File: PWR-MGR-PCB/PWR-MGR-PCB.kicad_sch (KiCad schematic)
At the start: 23 parts, among them J1 USB_C_Receptacle_USB2.0_14P, J2 Battery_1x2, U1 USBLC6-2SC6, U3 BQ24074RGT, U4 TPS631011YBGR

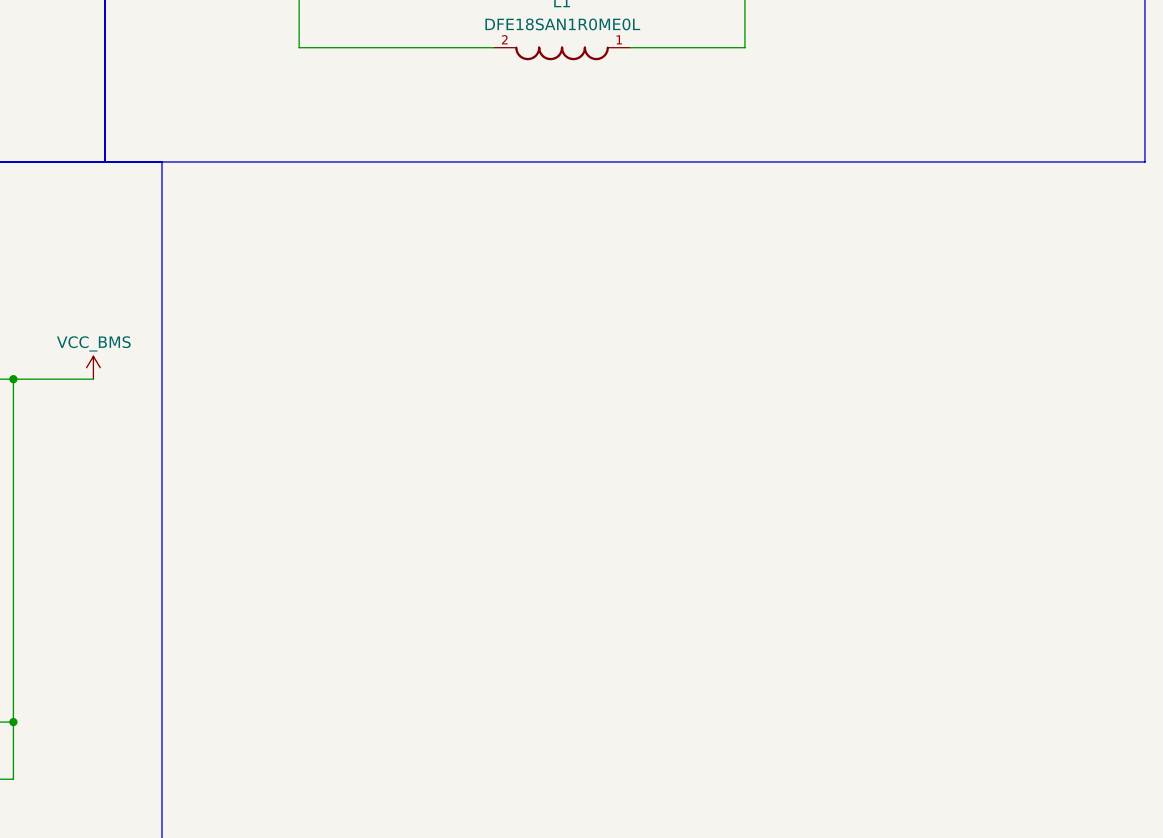
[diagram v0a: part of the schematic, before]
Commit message: Add USB lines, add mount holes, add power port
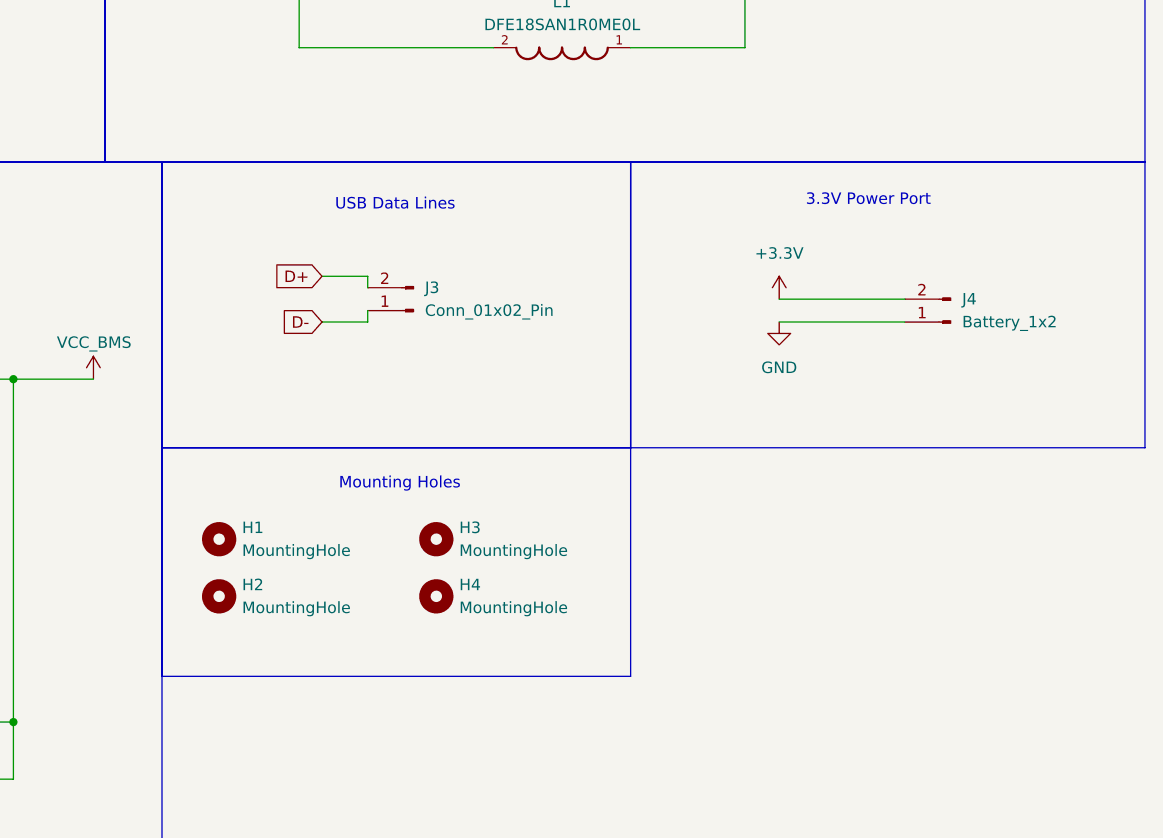
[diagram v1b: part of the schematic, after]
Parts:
- added H1, H2, H3, H4: MountingHole, MountingHole:MountingHole_2.1mm, symbol Mechanical:MountingHole
- added J3: Conn_01x02_Pin, Connector_PinHeader_1.00mm:PinHeader_1x02_P1.00mm_Vertical_SMD_Pin1Right, symbol Connector:Conn_01x02_Pin
- added J4: Battery_1x2, Connector_JST:JST_PH_B2B-PH-K_1x02_P2.00mm_Vertical, symbol Connector:Conn_01x02_Pin
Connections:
- net +3.3V: now also J4.2 (Pin_2)
- net D+: now also J3.2 (Pin_2)
- net D-: now also J3.1 (Pin_1)
- net GND: now also J4.1 (Pin_1)
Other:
- note added: "3.3V Power Port"
- note added: "Mounting Holes"
- note added: "USB Data Lines"

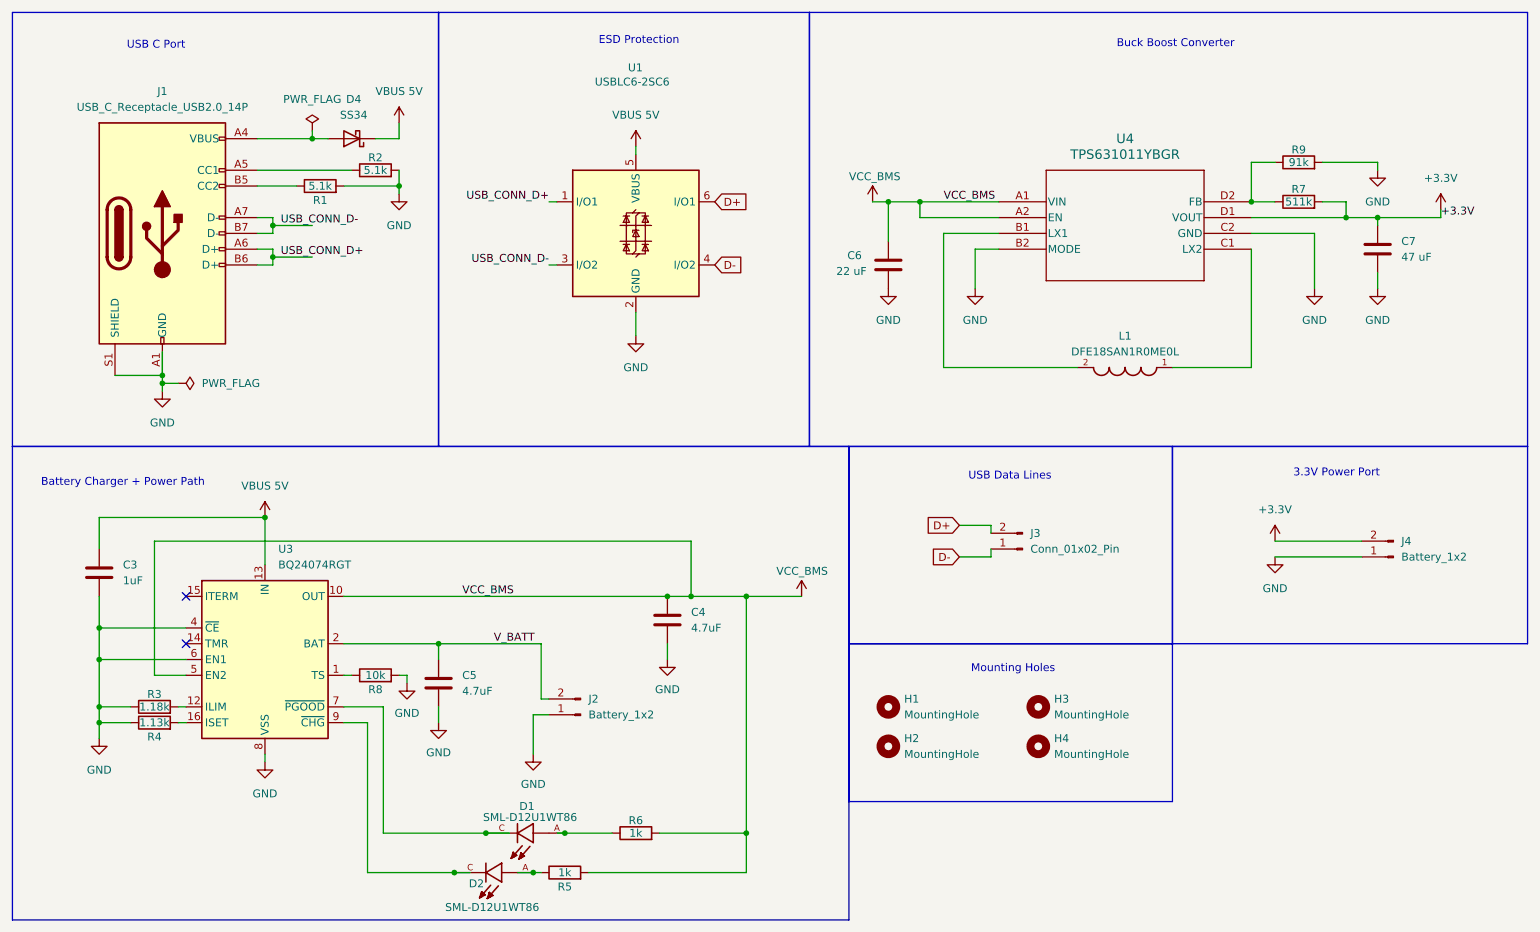
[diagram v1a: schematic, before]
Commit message: Format sheet for reusability
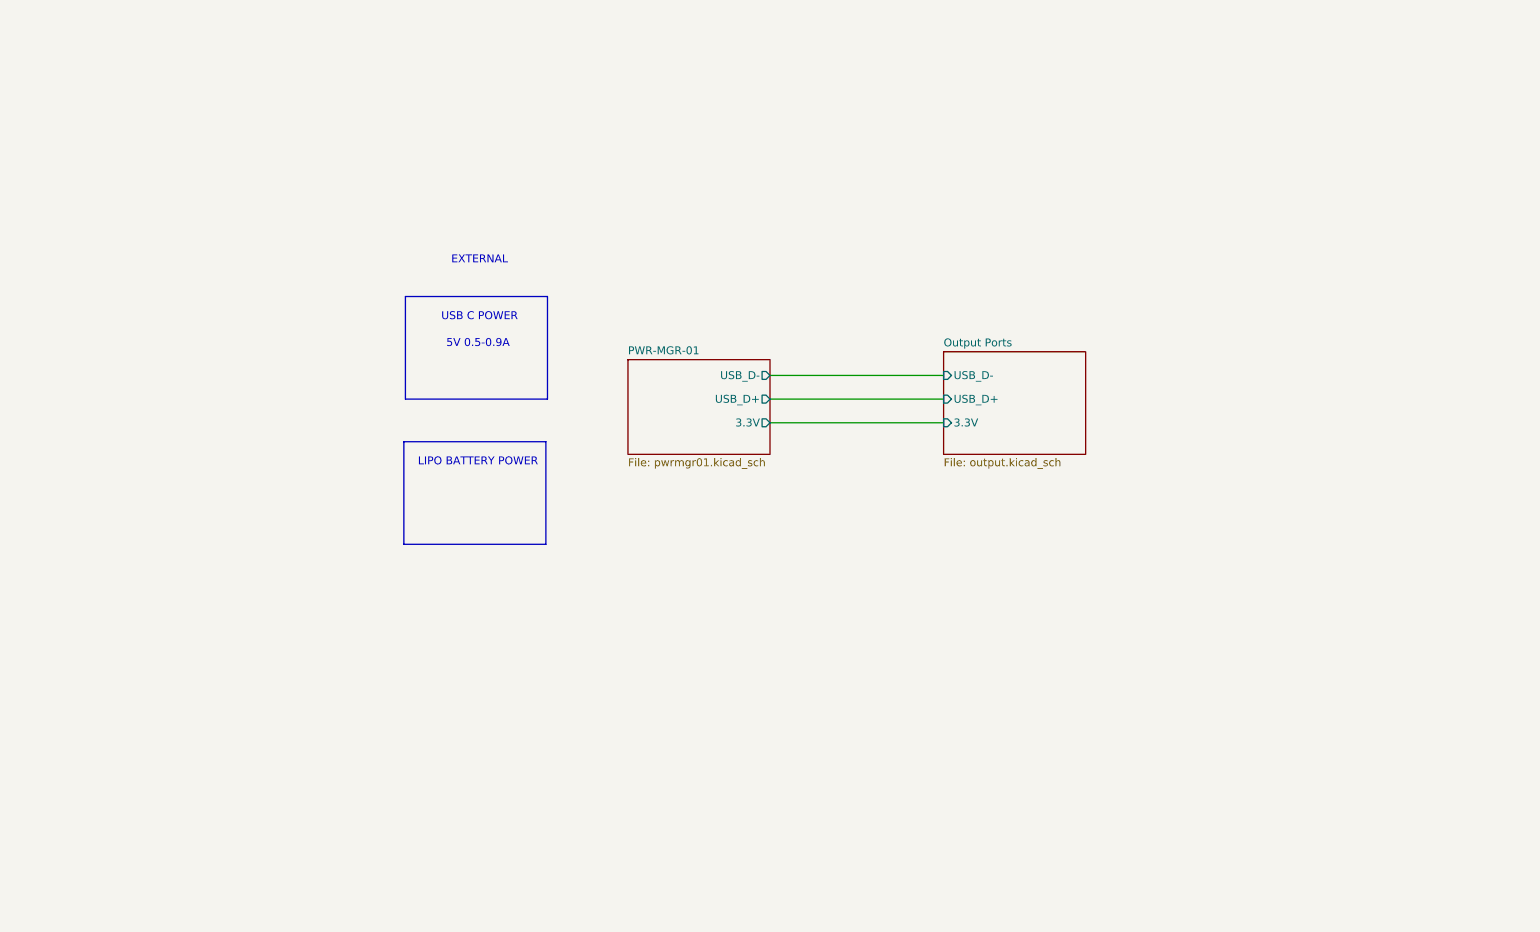
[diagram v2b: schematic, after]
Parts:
- removed C3: 1uF, Capacitor_SMD:C_0805_2012Metric, symbol Device:C
- removed C4, C5: 4.7uF, Capacitor_SMD:C_0805_2012Metric, symbol Device:C
- removed C6: 22 uF, Capacitor_SMD:C_0805_2012Metric, symbol Device:C
- removed C7: 47 uF, Capacitor_SMD:C_0805_2012Metric, symbol Device:C
- removed D1, D2: SML-D12U1WT86, LED - SML_D12U1WT86:LED_SML-D12U1WT86, symbol SML-D12U1WT86:SML-D12U1WT86
- removed D4: SS34, Diode_SMD:D_SMA, symbol Diode:SS34
- removed H1, H2, H3, H4: MountingHole, MountingHole:MountingHole_2.1mm, symbol Mechanical:MountingHole
- removed J1: USB_C_Receptacle_USB2.0_14P, Connector_USB:USB_C_Receptacle_GCT_USB4105-xx-A_16P_TopMnt_Horizontal, symbol Connector:USB_C_Receptacle_USB2.0_14P
- removed J2, J4: Battery_1x2, Connector_JST:JST_PH_B2B-PH-K_1x02_P2.00mm_Vertical, symbol Connector:Conn_01x02_Pin
- removed J3: Conn_01x02_Pin, Connector_PinHeader_1.00mm:PinHeader_1x02_P1.00mm_Vertical_SMD_Pin1Right, symbol Connector:Conn_01x02_Pin
- removed L1: DFE18SAN1R0ME0L, DFE18SAN1ROMEO Inductor:INDC1608X80N, symbol DFE18SAN1R0ME0L:DFE18SAN1R0ME0L
- removed R1, R2: 5.1k, Resistor_SMD:R_0805_2012Metric, symbol Device:R
- removed R3: 1.18k, Resistor_SMD:R_0805_2012Metric, symbol Device:R
- removed R4: 1.13k, Resistor_SMD:R_0805_2012Metric, symbol Device:R
- removed R5, R6: 1k, Resistor_SMD:R_0805_2012Metric, symbol Device:R
- removed R7: 511k, Resistor_SMD:R_0805_2012Metric, symbol Device:R
- removed R8: 10k, Resistor_SMD:R_0805_2012Metric, symbol Device:R
- removed R9: 91k, Resistor_SMD:R_0805_2012Metric, symbol Device:R
- removed U1: USBLC6-2SC6, Package_TO_SOT_SMD:SOT-23-6, symbol Power_Protection:USBLC6-2SC6
- removed U3: BQ24074RGT, BQ24074RGTR:QFN50P300X300X100-17N, symbol Battery_Management:BQ24074RGT
- removed U4: TPS631011YBGR, TPS631011 - Buck Boost Converter:DSBGA8_YBG_TEX, symbol TPS631011:TPS631011YBGR
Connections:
- no-connect marks 2 -> 0
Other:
- added sheet Output Ports (output.kicad_sch)
- added sheet PWR-MGR-01 (pwrmgr01.kicad_sch)
- note added: "5V 0.5-0.9A"
- note added: "EXTERNAL"
- note added: "LIPO BATTERY POWER"
- note added: "USB C POWER"
- note removed: "3.3V Power Port"
- note removed: "Battery Charger + Power Path"
- note removed: "Buck Boost Converter"
- note removed: "ESD Protection"
- note removed: "Mounting Holes"
- note removed: "USB C Port"
- note removed: "USB Data Lines"
- title: (none) -> PWR-MGR-PCB-01
